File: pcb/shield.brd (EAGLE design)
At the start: 53 x 53.3 mm, 10 parts, among them IC2 7805DT, U1 ARDUINO_SHIELDLABEL

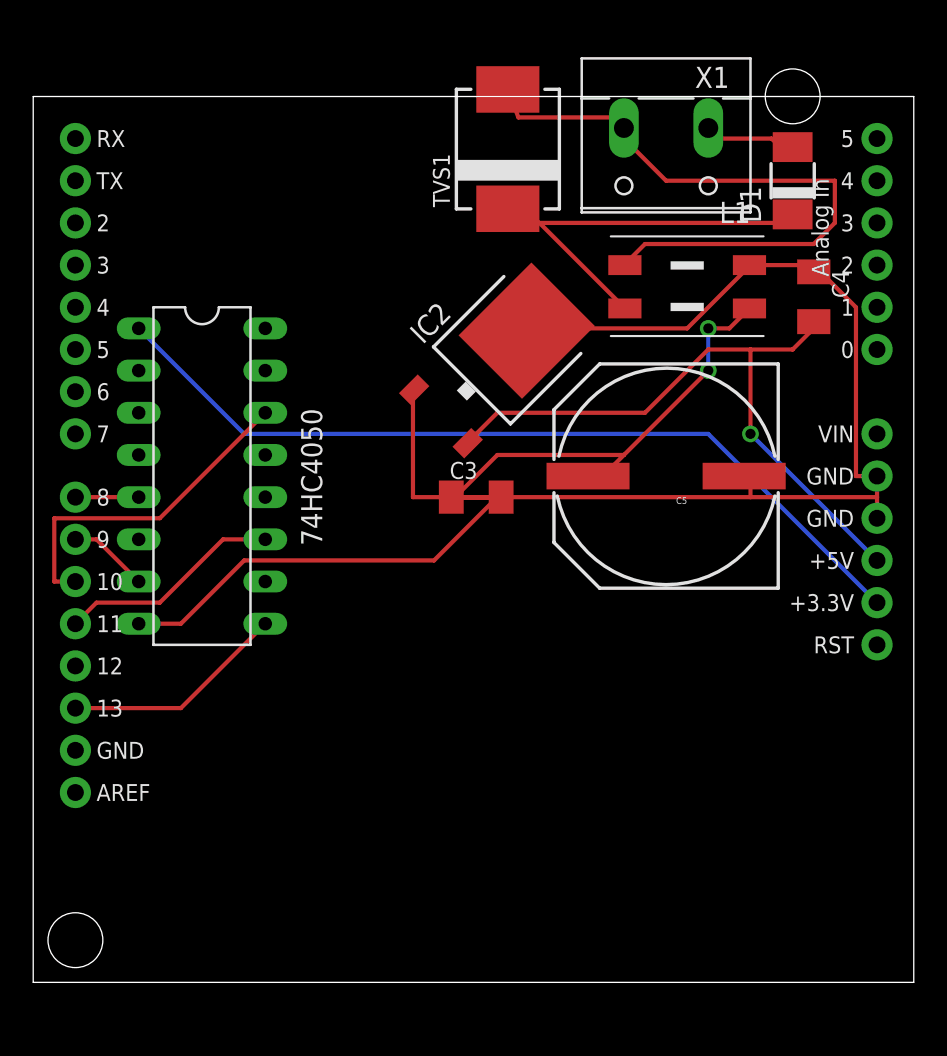
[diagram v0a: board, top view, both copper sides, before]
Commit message: moved the source and added pinheader for the display
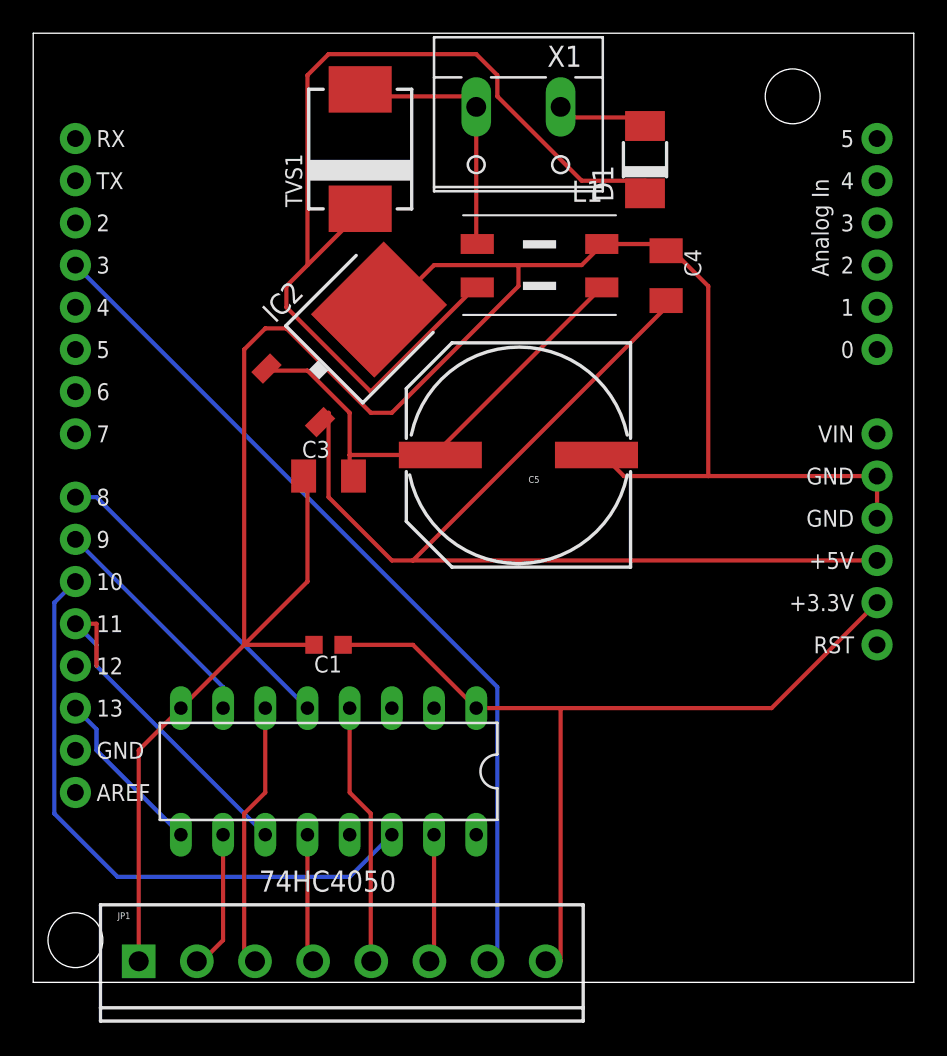
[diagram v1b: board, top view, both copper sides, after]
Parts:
- added C1: 100p, rcl:C0603K
- added JP1: (no value), SparkFun:SCREWTERMINAL-3.5MM-8
- C3, C4: value (none) -> 100n
- C5: value (none) -> 250µ
- moved 74HC4050 19.3 mm to (39.4, 34.3), turned to 180 degrees
- moved C3 8.98 mm to (39.4, 52.1)
- moved C4 8.98 mm to (59.7, 64.1)
- moved C5 8.98 mm to (50.8, 53.3)
- moved D1 8.98 mm to (58.4, 71.1)
- moved IC2 8.98 mm to (40.6, 60.3)
- moved L1 8.98 mm to (52.1, 64.8)
- moved X1 8.98 mm to (50.8, 73.7)
- moved TVS1 8.89 mm to (41.3, 71.8)
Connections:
- new net N$11: 74HC4050.6, JP1.3
- new net N$12: 74HC4050.12, JP1.4
- new net N$13: 74HC4050.4, JP1.5
- new net N$14: 74HC4050.15, JP1.6
- new net N$15: JP1.7, U1.D3
- new net N$8: 74HC4050.10, JP1.2
- net +3V3: now also C1.1, JP1.8
- net GND: now also C1.2, JP1.1
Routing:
- net N$15: track 0.00 -> 53.0 mm
- net GND: track 92.2 -> 134.0 mm
- net N$6: track 27.5 -> 60.9 mm
- net N$10: track 39.5 -> 16.1 mm
- net +5V: track 40.0 -> 62.4 mm, vias 1 -> 0
- net N$3: track 20.4 -> 37.4 mm
- net N$11: track 0.00 -> 16.4 mm
- net N$13: track 0.00 -> 15.8 mm
- net N$7: track 3.81 -> 19.2 mm
- net N$4: track 41.4 -> 30.6 mm, vias 2 -> 0
- net N$5: track 4.86 -> 13.8 mm
- net N$8: track 0.00 -> 8.46 mm
- net N$12: track 0.00 -> 7.96 mm
- net N$14: track 0.00 -> 7.90 mm
- net N$2: track 13.5 -> 21.2 mm
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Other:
- board size 53 x 53.3 mm -> 53 x 57.1 mm
